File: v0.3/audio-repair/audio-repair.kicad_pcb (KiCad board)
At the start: 2 copper layers, 50 x 50 mm, 32 parts, among them J2 Switchcraft_35RAPC4BHN3, J3 PL, J5 UVP, U1 PAM8019KGR, U2 1bitsy-basic-stubby

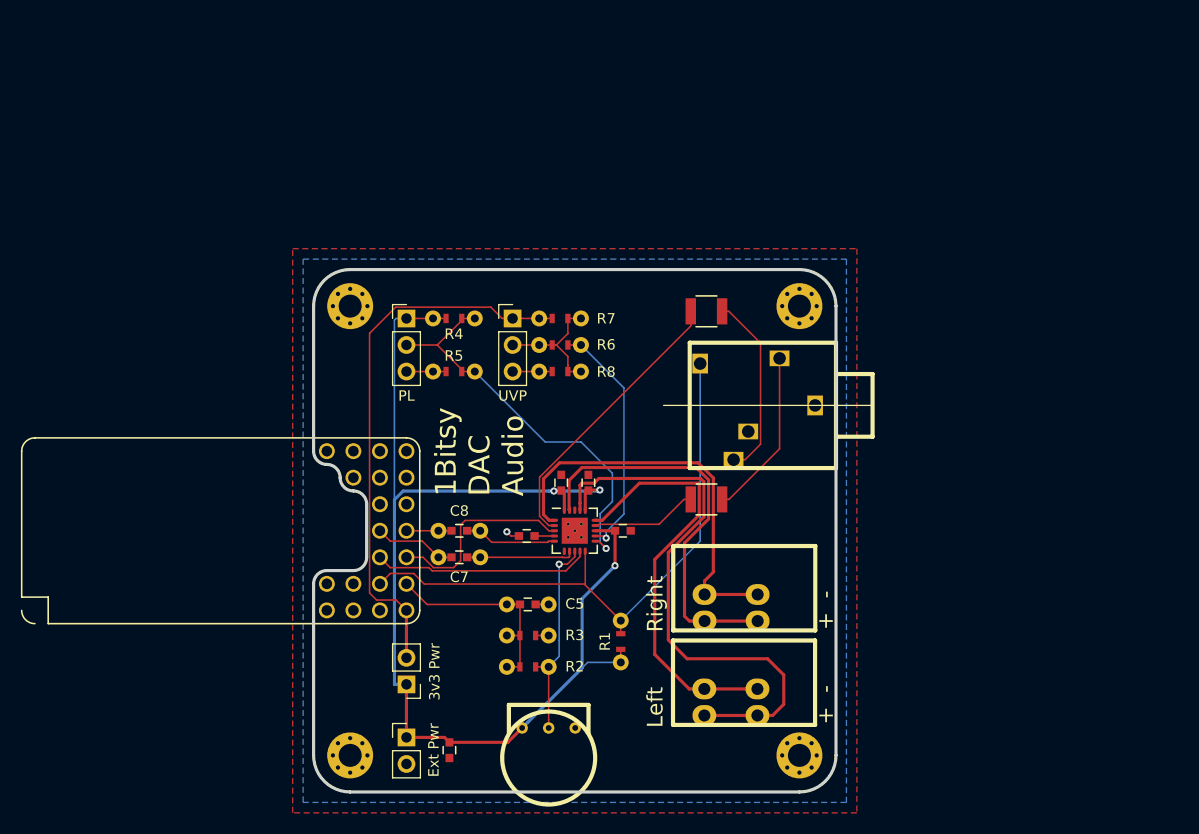
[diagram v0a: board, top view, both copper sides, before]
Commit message: lay out v0.3 board.
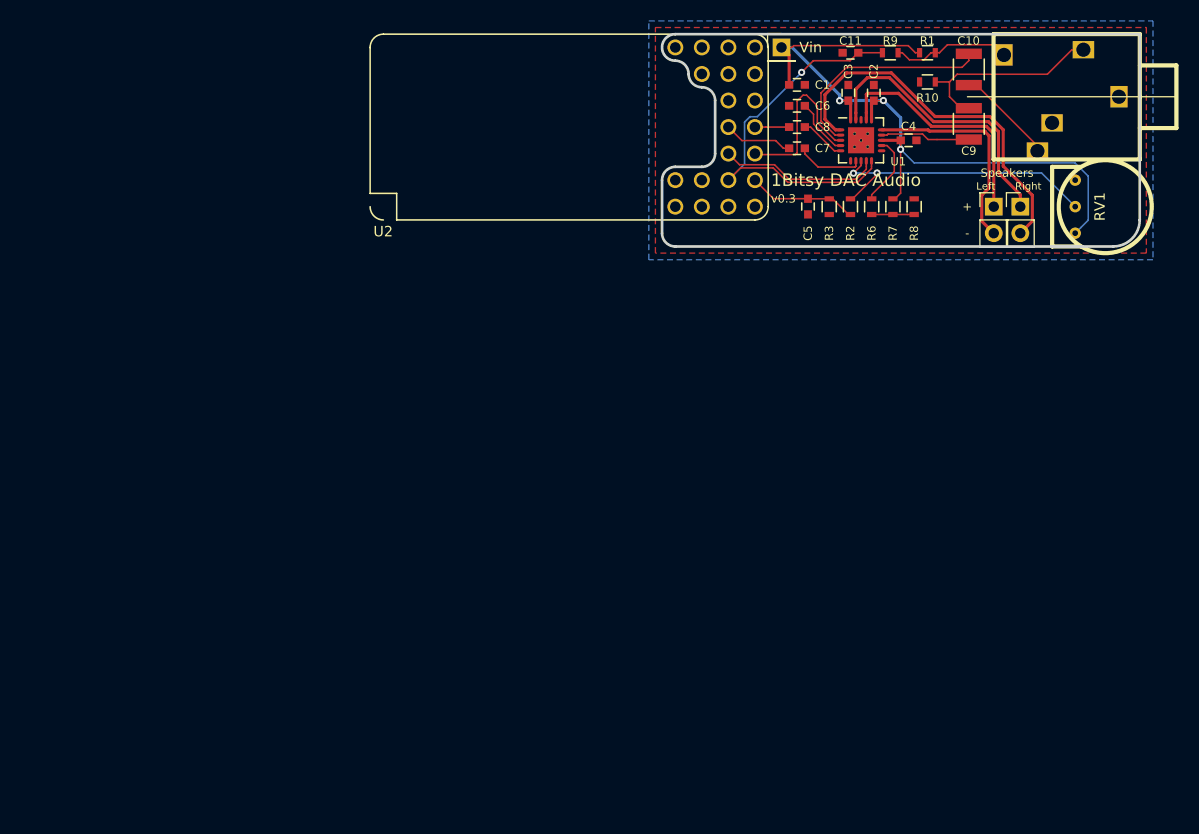
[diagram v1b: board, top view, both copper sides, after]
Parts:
- removed 3v3 Pwr: Jumper, Pin_Headers:Pin_Header_Straight_1x02_Pitch2.54mm
- removed Ext Pwr: Ext. Power, Pin_Headers:Pin_Header_Straight_1x02_Pitch2.54mm
- removed J3: PL, Pin_Headers:Pin_Header_Straight_1x03_Pitch2.54mm
- removed J5: UVP, Pin_Headers:Pin_Header_Straight_1x03_Pitch2.54mm
- removed Left, Right: Speaker, audio-repair:TerminalBlock_TE_2834016_2
- removed R4, R5: TBD, audio-repair:R_0603_TH_unpop
- removed REF** (x4): MountingHole_2.2mm_M2_Pad_Via, audio-repair:MountingHole_2.2mm_M2_Pad_Via
- added C11: 100nF, Capacitors_SMD:C_0603, F.Cu at (151.4, 79.2)
- added J1: Vin, Pin_Headers:Pin_Header_Straight_1x01_Pitch2.54mm, F.Cu at (144.8, 78.7)
- added J4: Left, Pin_Headers:Pin_Header_Straight_1x02_Pitch2.54mm, F.Cu at (165.1, 94.0)
- added J6: Right, Pin_Headers:Pin_Header_Straight_1x02_Pitch2.54mm, F.Cu at (167.6, 94.0)
- added R10: 10K, Resistors_SMD:R_0603, F.Cu at (158.8, 82.0)
- added R9: 51K, Resistors_SMD:R_0603, F.Cu at (155.2, 79.2)
- C5, C7, C8: footprint audio-repair:C_0603_TH -> Capacitors_SMD:C_0603
- R1, R2, R3: footprint audio-repair:R_0603_TH -> Resistors_SMD:R_0603
- R6: value 100K -> 33K; footprint audio-repair:R_0603_TH -> Resistors_SMD:R_0603
- R7: value TBD -> 18K; footprint audio-repair:R_0603_TH_unpop -> Resistors_SMD:R_0603
- R8: value TBD -> 33K; footprint audio-repair:R_0603_TH_unpop -> Resistors_SMD:R_0603
- moved RV1 75.0 mm to (175.8, 94.0), turned to 270 degrees
- moved C1 71.8 mm to (146.3, 82.3), turned to 0 degrees
- moved R1 65.3 mm to (158.8, 79.2), turned to 0 degrees
- moved R2 52.7 mm to (151.4, 94.0), turned to 270 degrees
- moved R3 51.3 mm to (149.4, 94.0), turned to 270 degrees
- moved U2 51.0 mm to (106.7, 94.0)
- moved C7 49.5 mm to (146.3, 88.4)
- moved C8 49.1 mm to (146.3, 86.4)
- moved C6 48.6 mm to (146.3, 84.3)
- moved C5 47.8 mm to (147.3, 94.0), turned to 270 degrees
- moved C3 46.3 mm to (151.2, 83.1)
- moved U1 46.3 mm to (152.4, 87.6)
- moved C4 46.3 mm to (156.9, 87.6)
- moved C2 46.2 mm to (153.6, 83.1)
- moved C9 43.8 mm to (162.7, 86.1), turned to 90 degrees
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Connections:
- J2 pad 4: /TIP_SW -> Net-(J2-Pad4)
- R1 pad 2: /TIP_SW -> Net-(J2-Pad4)
- R7 pad 1: +3V3 -> VDD
- U1 pad 11: Net-(J3-Pad2) -> GND
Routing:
- net +3V3: track 52.6 -> 0.00 mm
- net VDD: track 113.8 -> 73.5 mm
- net Net-(J3-Pad2): track 38.9 -> 0.00 mm, vias 1 -> 0
- net Net-(J4-Pad1): track 54.5 -> 23.3 mm
- net Net-(J4-Pad2): track 40.7 -> 20.7 mm
- net /TIP_SW: track 57.5 -> 38.2 mm, vias 0 -> 1
- net Net-(R6-Pad2): track 23.3 -> 6.80 mm, vias 1 -> 0
- net Net-(J2-Pad4): track 0.00 -> 11.6 mm
- net GND: track 11.4 -> 0.00 mm, vias 1 -> 0
- net Net-(J6-Pad1): track 38.4 -> 27.2 mm
- net /VOL_ADC: track 20.2 -> 10.5 mm
- net Net-(R6-Pad1): track 12.7 -> 4.06 mm
- net Net-(C10-Pad2): track 17.8 -> 9.47 mm
- net Net-(R2-Pad1): track 19.7 -> 27.7 mm, vias 1 -> 2
- net Net-(C10-Pad1): track 27.4 -> 21.2 mm
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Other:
- board size 50 x 50 mm -> 45.7 x 20.3 mm
- net class Speaker removed
- net class Speaker Wire added: clearance 0.1524, trace_width 0.3, via_dia 0.6858, via_drill 0.3302
- rule pad_to_mask_clearance: 0 -> 0.0508
- board text added: "Speakers"
- board text added: "This board is upside down."
- board text added: "v0.3"
